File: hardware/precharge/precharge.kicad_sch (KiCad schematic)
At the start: 38 parts, among them J1 Conn_01x02, J2 Conn_01x02, J3 Conn_01x02, J4 Conn_01x04, J5 Conn_01x03, J6 Conn_01x05, U1 140817141410, U2 140817141410, U3 140817141410

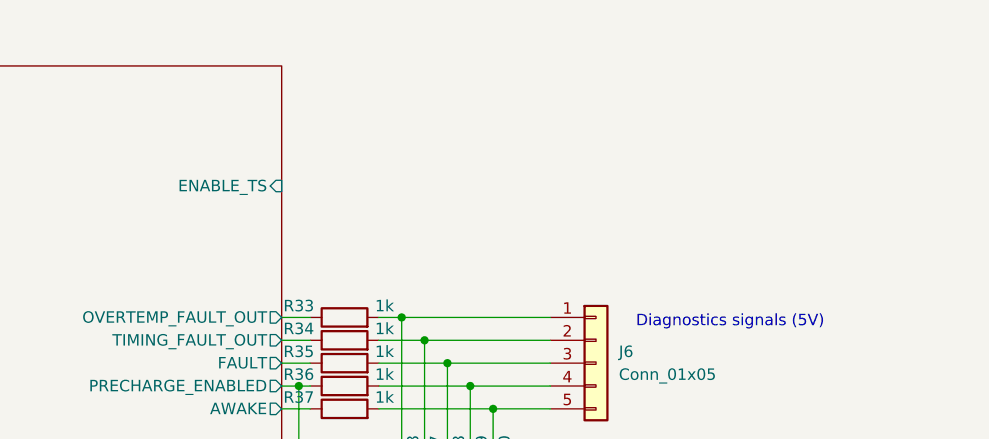
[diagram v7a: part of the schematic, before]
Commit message: Restarted PCB layout
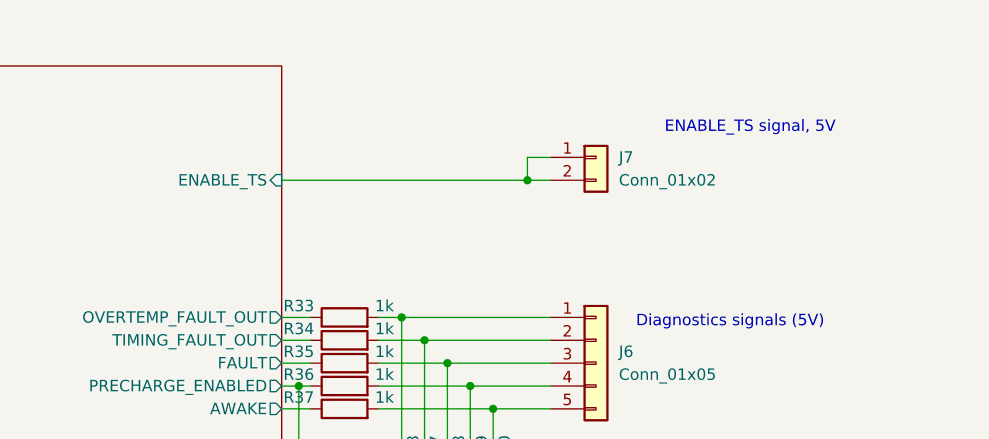
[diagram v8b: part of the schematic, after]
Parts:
- added J7: Conn_01x02, Connector_Molex:Molex_Micro-Fit_3.0_43650-0200_1x02_P3.00mm_Horizontal, symbol Connector_Generic:Conn_01x02
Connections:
- net LV side/ENABLE_TS: now also J7.1 (Pin_1), J7.2 (Pin_2)
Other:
- note added: "ENABLE_TS signal, 5V"
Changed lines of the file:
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@@
   (junction (at 222.25 55.245) (diameter 0) (color 0 0 0 0)
+  )
+  (junction (at 236.22 40.005) (diameter 0) (color 0 0 0 0)
   )
   (junction (at 224.155 132.08) (diameter 0) (color 0 0 0 0)
@@
     (stroke (width 0) (type default) (color 0 0 0 0))
   )
+  (wire (pts (xy 208.915 40.005) (xy 236.22 40.005))
+    (stroke (width 0) (type default) (color 0 0 0 0))
+  )
   (wire (pts (xy 104.14 65.405) (xy 107.315 65.405))
     (stroke (width 0) (type default) (color 0 0 0 0))
@@
     (stroke (width 0) (type default) (color 0 0 0 0))
   )
+  (wire (pts (xy 236.22 37.465) (xy 236.22 40.005))
+    (stroke (width 0) (type default) (color 0 0 0 0))
+  )
   (wire (pts (xy 85.09 65.405) (xy 85.09 67.31))
     (stroke (width 0) (type default) (color 0 0 0 0))
@@
     (stroke (width 0) (type default) (color 0 0 0 0))
   )
+  (wire (pts (xy 236.22 40.005) (xy 238.76 40.005))
+    (stroke (width 0) (type default) (color 0 0 0 0))
+  )
   (wire (pts (xy 219.71 57.785) (xy 224.79 57.785))
     (stroke (width 0) (type default) (color 0 0 0 0))
@@
   )
   (wire (pts (xy 132.715 36.83) (xy 136.525 36.83))
+    (stroke (width 0) (type default) (color 0 0 0 0))
+  )
+  (wire (pts (xy 238.76 37.465) (xy 236.22 37.465))
     (stroke (width 0) (type default) (color 0 0 0 0))
   )
@@
   )
   (text "Precharge relay coil" (at 121.285 46.355 90)
+    (effects (font (size 1.27 1.27)) (justify left bottom))
+  )
+  (text "ENABLE_TS signal, 5V" (at 251.46 34.925 0)
     (effects (font (size 1.27 1.27)) (justify left bottom))
   )
@@
     )
     (property "Datasheet" "~" (id 3) (at 232.41 74.295 0)
+      (effects (font (size 1.27 1.27)) hide)
+    )
+    (pin "1")
+    (pin "2")
+  )
+  (symbol (lib_id "Connector_Generic:Conn_01x02") (at 243.84 37.465 0) (unit 1)
+    (in_bom yes) (on_board yes) (fields_autoplaced)
+    (property "Reference" "J7" (id 0) (at 246.38 37.4649 0)
+      (effects (font (size 1.27 1.27)) (justify left))
+    )
+    (property "Value" "Conn_01x02" (id 1) (at 246.38 40.0049 0)
+      (effects (font (size 1.27 1.27)) (justify left))
+    )
+    (property "Footprint" "Connector_Molex:Molex_Micro-Fit_3.0_43650-0200_1x02_P3.00mm_Horizontal" (id 2) (at 243.84 37.465 0)
+      (effects (font (size 1.27 1.27)) hide)
+    )
+    (property "Datasheet" "~" (id 3) (at 243.84 37.465 0)
       (effects (font (size 1.27 1.27)) hide)
     )
@@
       (effects (font (size 1.27 1.27)) (justify left))
     )
-    (pin "ENABLE_TS" input (at 208.915 40.64 0)
+    (pin "ENABLE_TS" input (at 208.915 40.005 0)
       (effects (font (size 1.27 1.27)) (justify right))
     )
@@
       (reference "J6") (unit 1) (value "Conn_01x05") (footprint "Connector_Molex:Molex_Micro-Fit_3.0_43650-0500_1x05_P3.00mm_Horizontal")
     )
+    (path "/e3a45e04-17e3-484c-934b-21af878704ca"
+      (reference "J7") (unit 1) (value "Conn_01x02") (footprint "Connector_Molex:Molex_Micro-Fit_3.0_43650-0200_1x02_P3.00mm_Horizontal")
+    )
     (path "/a25b3faf-d95a-49ad-9b40-7c3f8d869233/0eaa663a-c98d-44db-8bf5-70ab2ac22caf"
       (reference "K2") (unit 1) (value "G5Q-1EU DC12") (footprint "Relay_THT:Relay_SPDT_Omron-G5Q-1")
@@
     )
     (path "/86ebb052-21e6-4e49-945d-049a70338ab6/1d8a2ff3-1a11-40af-b965-a214345cb0c2"
-      (reference "R51") (unit 1) (value "453k") (footprint "Resistor_SMD:R_0805_2012Metric")
+      (reference "R51") (unit 1) (value "470k") (footprint "Resistor_SMD:R_0603_1608Metric")
     )
     (path "/86ebb052-21e6-4e49-945d-049a70338ab6/ec6b5a51-4fa3-4070-a193-4983450afaaf"
